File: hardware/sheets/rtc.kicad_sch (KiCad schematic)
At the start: 9 parts, among them U1 DS12C887, U2 74HCT138, U3 74HC02, U4 74HC08, U5 74HC32, U6 74HC04

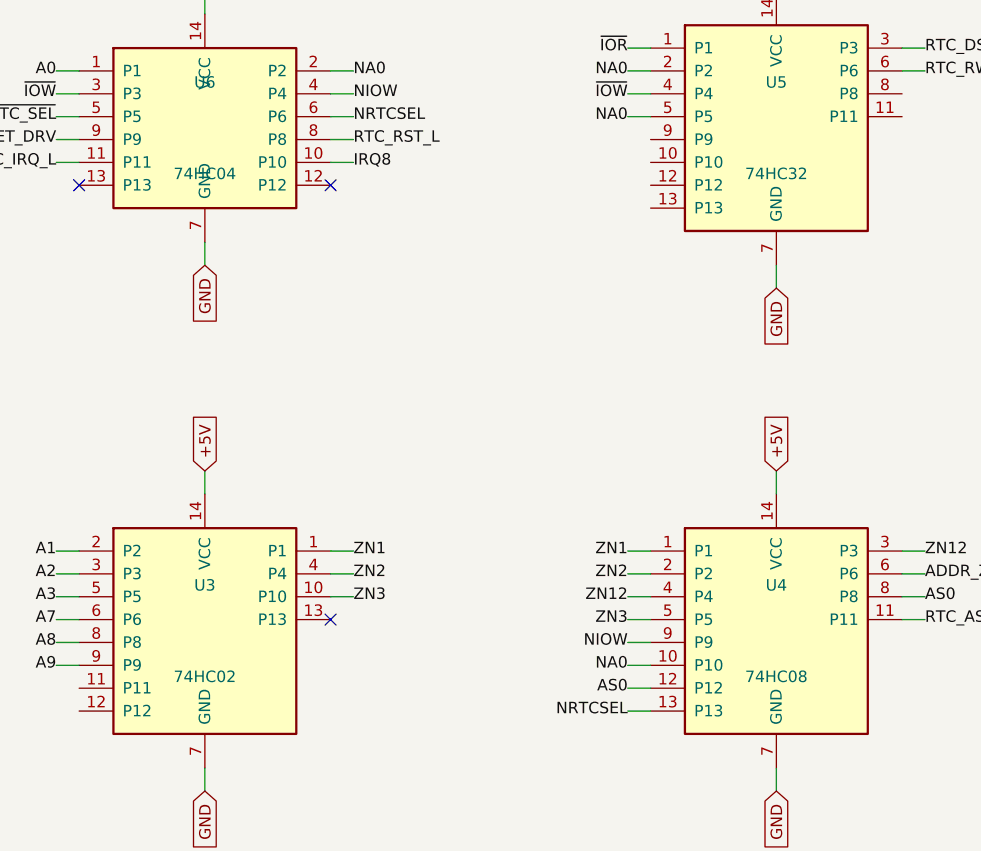
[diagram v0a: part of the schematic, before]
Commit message: Standardize 5V glue on 74HCT; fix bus-latch family; div-3 -> 74HCT163
All 5V 74-series logic moved from mixed HC/HCT to 74HCT (TTL thresholds reliably
read 3.3V level-shifter outputs). Fixes the address latches / data transceiver
that were wrongly 74HC instead of the design's 74HCT. The div-by-3 moves from
74HC4017 (no HCT variant) to a 74HCT163 preset-to-3 with a spare 74HCT04 gate
for the TC->~PE reload. Per-card level shifters use a dedicated 74LVC245A symbol.
Pinouts unchanged; netlist intact; zero structural ERC errors.

Co-Authored-By: Claude Opus 4.8 (1M context) <noreply@anthropic.com>
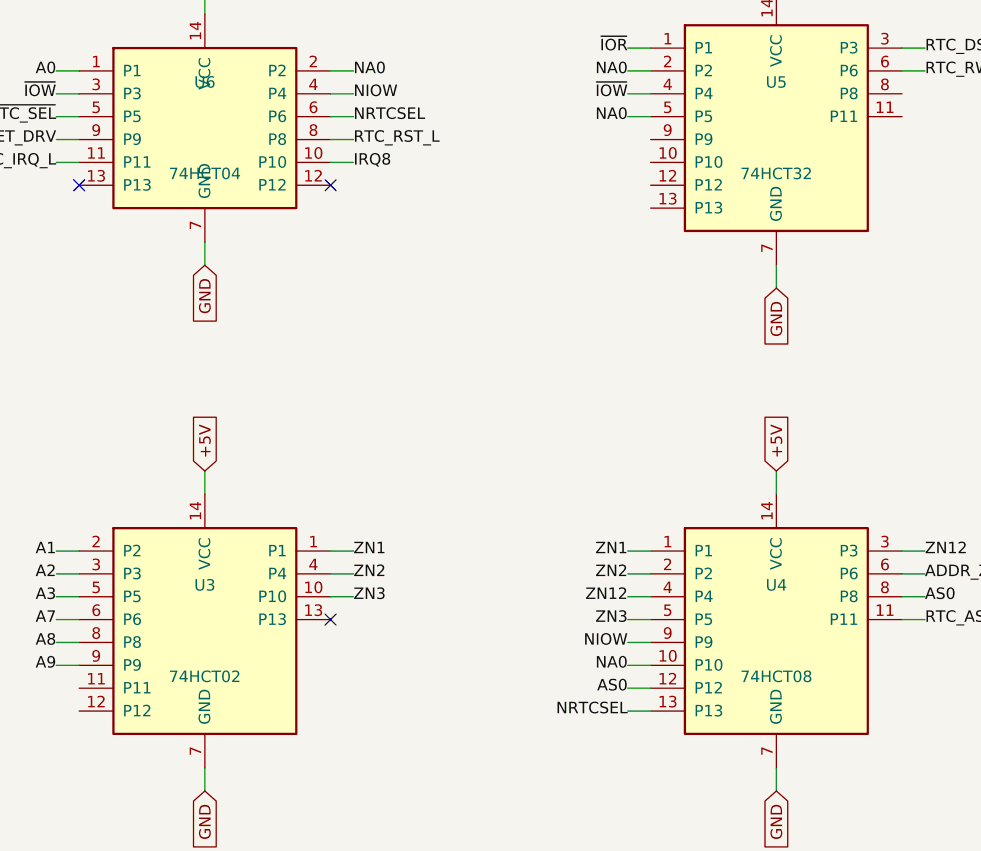
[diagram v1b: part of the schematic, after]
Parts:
- removed U3: 74HC02, symbol mini-xt:74HC02
- removed U4: 74HC08, symbol mini-xt:74HC08
- removed U5: 74HC32, symbol mini-xt:74HC32
- removed U6: 74HC04, symbol mini-xt:74HC04
- added U3: 74HCT02, symbol mini-xt:74HCT02
- added U4: 74HCT08, symbol mini-xt:74HCT08
- added U5: 74HCT32, symbol mini-xt:74HCT32
- added U6: 74HCT04, symbol mini-xt:74HCT04
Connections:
- net +5V: now also U3.14 (VCC), U4.14 (VCC), U5.14 (VCC), U6.14 (VCC)
- net A0: now also U6.1 (P1)
- net A1: now also U3.2 (P2)
- net A2: now also U3.3 (P3)
- net A3: now also U3.5 (P5)
- net A7: now also U3.6 (P6)
- net A8: now also U3.8 (P8)
- net A9: now also U3.9 (P9)
- net ADDR_ZERO: now also U4.6 (P6)
- net AS0: now also U4.12 (P12), U4.8 (P8)
- net GND: now also U3.7 (GND), U4.7 (GND), U5.7 (GND), U6.7 (GND)
- net IRQ8: now also U6.10 (P10)
- net NA0: now also U4.10 (P10), U5.2 (P2), U5.5 (P5), U6.2 (P2)
- net NIOW: now also U4.9 (P9), U6.4 (P4)
- net NRTCSEL: now also U4.13 (P13), U6.6 (P6)
- net RESET_DRV: now also U6.9 (P9)
- net RTC_AS: now also U4.11 (P11)
- net RTC_DS: now also U5.3 (P3)
- net RTC_IRQ_L: now also U6.11 (P11)
- net RTC_RST_L: now also U6.8 (P8)
- net RTC_RW: now also U5.6 (P6)
- net ZN1: now also U3.1 (P1), U4.1 (P1)
- net ZN12: now also U4.3 (P3), U4.4 (P4)
- net ZN2: now also U3.4 (P4), U4.2 (P2)
- net ZN3: now also U3.10 (P10), U4.5 (P5)
- net ~{IOR}: now also U5.1 (P1)
- net ~{IOW}: now also U5.4 (P4), U6.3 (P3)
- net ~{RTC_SEL}: now also U6.5 (P5)
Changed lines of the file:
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@@
 		(instances
 			(project "mini-xt"
-				(path "/d5fb706d-3720-437f-850e-91a8fdce298f/94459517-8f52-4b71-b7cf-077d720bb37e"
+				(path "/12a90590-121b-4b08-bc73-62c223de1072/c3feead8-4c72-4521-88a9-7d04724877bf"
 					(reference "U801")
 					(unit 1)
@@
 		(instances
 			(project "mini-xt"
-				(path "/d5fb706d-3720-437f-850e-91a8fdce298f/94459517-8f52-4b71-b7cf-077d720bb37e"
+				(path "/12a90590-121b-4b08-bc73-62c223de1072/c3feead8-4c72-4521-88a9-7d04724877bf"
 					(reference "R801")
 					(unit 1)
@@
 		(instances
 			(project "mini-xt"
-				(path "/d5fb706d-3720-437f-850e-91a8fdce298f/94459517-8f52-4b71-b7cf-077d720bb37e"
+				(path "/12a90590-121b-4b08-bc73-62c223de1072/c3feead8-4c72-4521-88a9-7d04724877bf"
 					(reference "U802")
 					(unit 1)
@@
 	)
 	(symbol
-		(lib_id "mini-xt:74HC02")
+		(lib_id "mini-xt:74HCT02")
 		(at 88.9 215.9 0)
 		(unit 1)
@@
 			)
 		)
-		(property "Value" "74HC02"
+		(property "Value" "74HCT02"
 			(at 88.9 220.98 0)
 			(effects
@@
 		(instances
 			(project "mini-xt"
-				(path "/d5fb706d-3720-437f-850e-91a8fdce298f/94459517-8f52-4b71-b7cf-077d720bb37e"
+				(path "/12a90590-121b-4b08-bc73-62c223de1072/c3feead8-4c72-4521-88a9-7d04724877bf"
 					(reference "U803")
 					(unit 1)
@@
 	)
 	(symbol
-		(lib_id "mini-xt:74HC08")
+		(lib_id "mini-xt:74HCT08")
 		(at 152.4 215.9 0)
 		(unit 1)
@@
 			)
 		)
-		(property "Value" "74HC08"
+		(property "Value" "74HCT08"
 			(at 152.4 220.98 0)
 			(effects
@@
 		(instances
 			(project "mini-xt"
-				(path "/d5fb706d-3720-437f-850e-91a8fdce298f/94459517-8f52-4b71-b7cf-077d720bb37e"
+				(path "/12a90590-121b-4b08-bc73-62c223de1072/c3feead8-4c72-4521-88a9-7d04724877bf"
 					(reference "U804")
 					(unit 1)
@@
 	)
 	(symbol
-		(lib_id "mini-xt:74HC32")
+		(lib_id "mini-xt:74HCT32")
 		(at 152.4 160.02 0)
 		(unit 1)
@@
 			)
 		)
-		(property "Value" "74HC32"
+		(property "Value" "74HCT32"
 			(at 152.4 165.1 0)
 			(effects
@@
 		(instances
 			(project "mini-xt"
-				(path "/d5fb706d-3720-437f-850e-91a8fdce298f/94459517-8f52-4b71-b7cf-077d720bb37e"
+				(path "/12a90590-121b-4b08-bc73-62c223de1072/c3feead8-4c72-4521-88a9-7d04724877bf"
 					(reference "U805")
 					(unit 1)
@@
 	)
 	(symbol
-		(lib_id "mini-xt:74HC04")
+		(lib_id "mini-xt:74HCT04")
 		(at 88.9 160.02 0)
 		(unit 1)
@@
 			)
 		)
-		(property "Value" "74HC04"
+		(property "Value" "74HCT04"
 			(at 88.9 165.1 0)
 			(effects
@@
 		(instances
 			(project "mini-xt"
-				(path "/d5fb706d-3720-437f-850e-91a8fdce298f/94459517-8f52-4b71-b7cf-077d720bb37e"
+				(path "/12a90590-121b-4b08-bc73-62c223de1072/c3feead8-4c72-4521-88a9-7d04724877bf"
 					(reference "U806")
 					(unit 1)
@@
 		(instances
 			(project "mini-xt"
-				(path "/d5fb706d-3720-437f-850e-91a8fdce298f/94459517-8f52-4b71-b7cf-077d720bb37e"
+				(path "/12a90590-121b-4b08-bc73-62c223de1072/c3feead8-4c72-4521-88a9-7d04724877bf"
 					(reference "C801")
 					(unit 1)
@@
 		(instances
 			(project "mini-xt"
-				(path "/d5fb706d-3720-437f-850e-91a8fdce298f/94459517-8f52-4b71-b7cf-077d720bb37e"
+				(path "/12a90590-121b-4b08-bc73-62c223de1072/c3feead8-4c72-4521-88a9-7d04724877bf"
 					(reference "C802")
 					(unit 1)
